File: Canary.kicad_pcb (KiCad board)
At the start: 4 copper layers, 56 x 38 mm, 92 parts, among them J1 CONN_ARM_CM_JTAG_SWD_10, J2 20021311-00010T4LF, J3 USB4125-GF-A, J4 S2B-PH-SM4-TB, Q1 PMN30UNX, Q2 PMN42XPEAH, Q3 PMN30UNX, SW1 TL3301SPF160QJ, U1 BMD-300-A-R, U10 LP5907MFX-3.2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

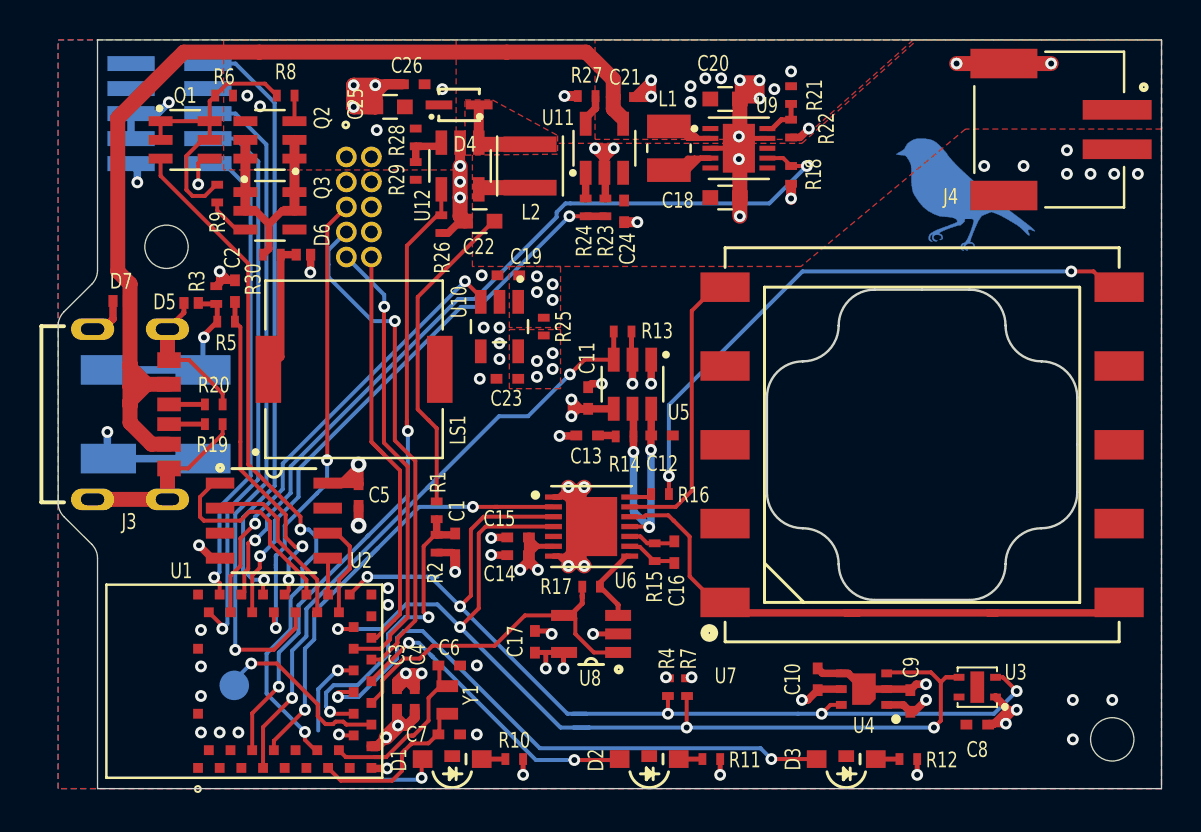
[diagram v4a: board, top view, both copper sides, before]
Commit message: Clean up silks, add fiducials
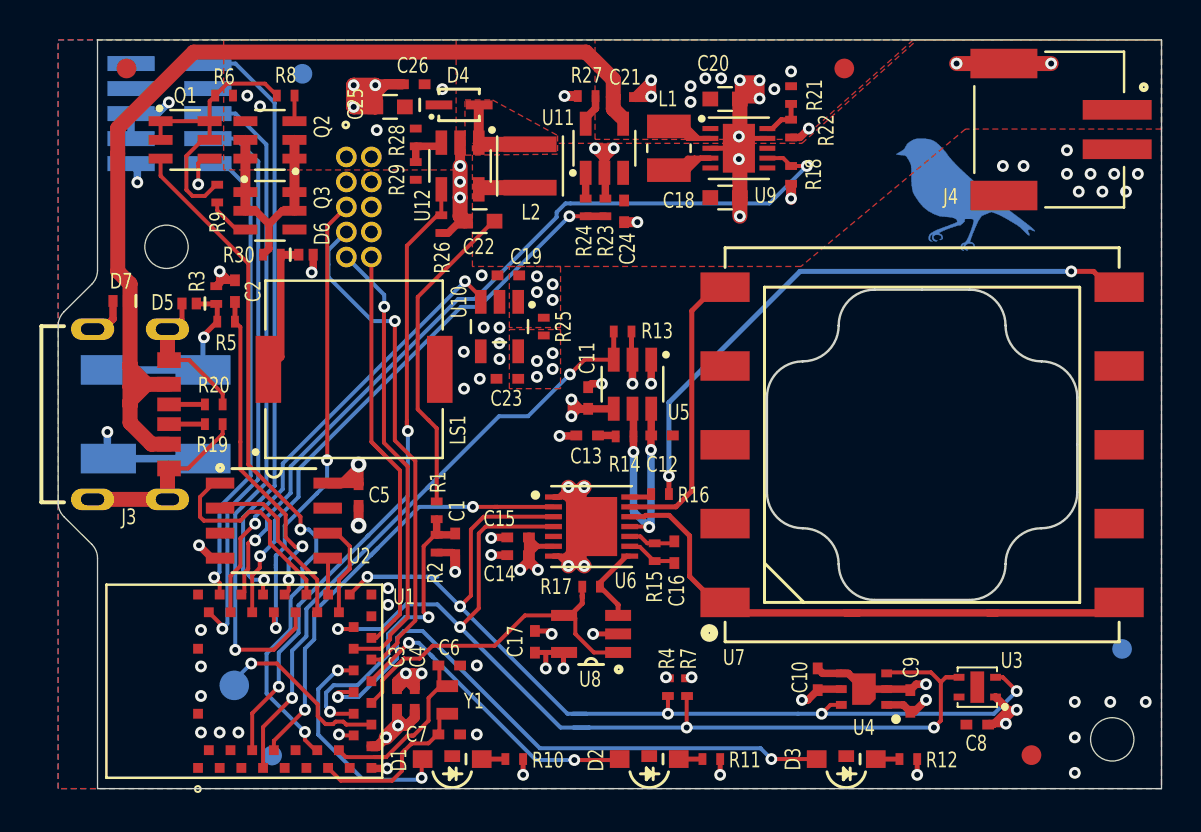
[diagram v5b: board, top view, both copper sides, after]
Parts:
- added FID1: Fiducial, Fiducials:Fiducial_1mm_Dia_2mm_Outer, F.Cu at (80.9, 49.5)
- added FID2: Fiducial, Fiducials:Fiducial_1mm_Dia_2mm_Outer, F.Cu at (90.4, 84.3)
- added FID3: Fiducial, Fiducials:Fiducial_1mm_Dia_2mm_Outer, F.Cu at (44.5, 49.5)
- added FID4: Fiducial, Fiducials:Fiducial_1mm_Dia_2mm_Outer, B.Cu at (95.0, 78.9)
- added FID5: Fiducial, Fiducials:Fiducial_1mm_Dia_2mm_Outer, B.Cu at (51.9, 84.3)
- added FID6: Fiducial, Fiducials:Fiducial_1mm_Dia_2mm_Outer, B.Cu at (53.4, 49.7)
- moved D6 0.13 mm to (53.6, 58.9)
- moved D5 0.10 mm to (47.6, 61.4)
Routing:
- net VBUS: track 57.8 -> 53.3 mm
- net LED_GREEN: track 8.06 -> 11.9 mm
- net /Potentiostat/SPEC_WE: track 29.0 -> 31.4 mm
- net /Potentiostat/SPEC_RE: track 14.4 -> 16.6 mm
- net /Potentiostat/SPEC_CE: track 30.1 -> 31.8 mm
- net /PDRIVE_O: track 8.26 -> 9.18 mm
- net GND: track 122.9 -> 123.0 mm, vias 75 -> 82

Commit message: Prepare for fab export
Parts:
- moved S1 0.43 mm to (50.3, 48.5)

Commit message: Generate gerbers
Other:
- rule pad_to_mask_clearance: 0.05 -> 0

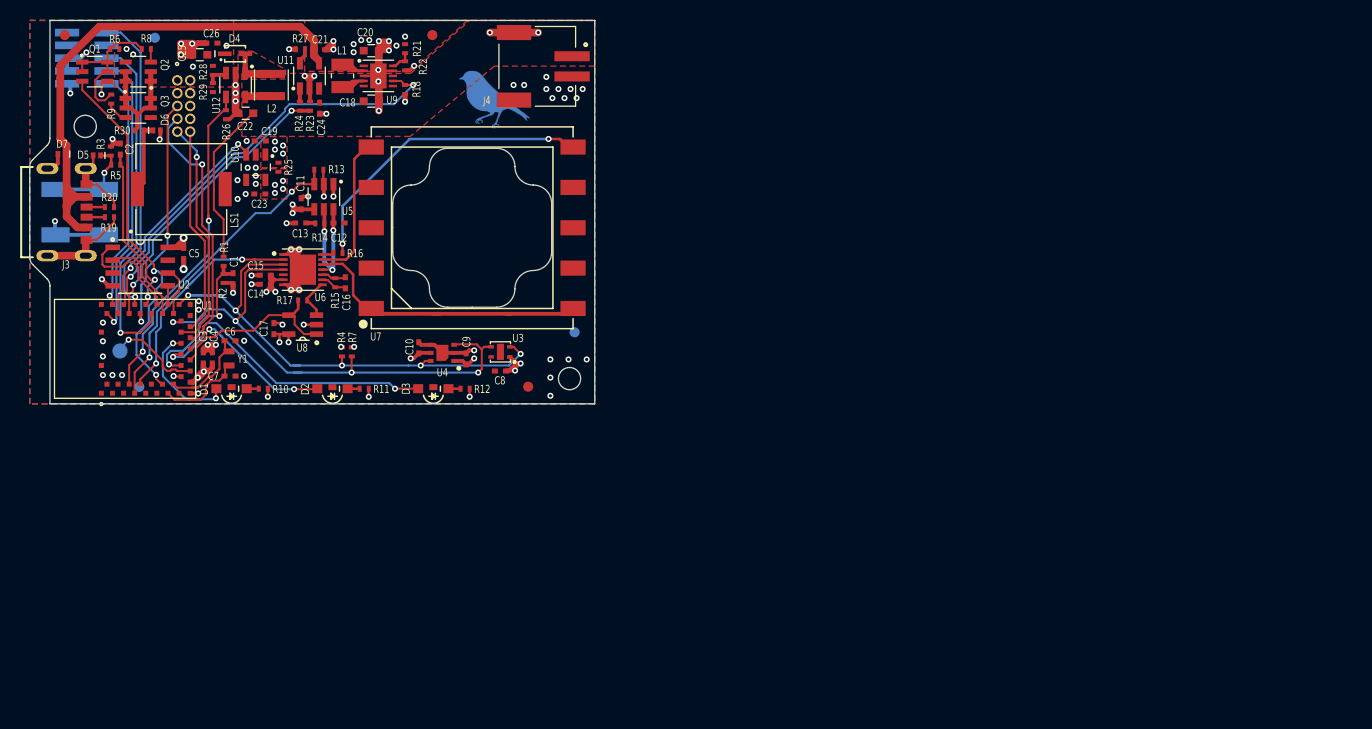
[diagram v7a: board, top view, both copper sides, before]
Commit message: Regenerate Gerbers using PCBWay process
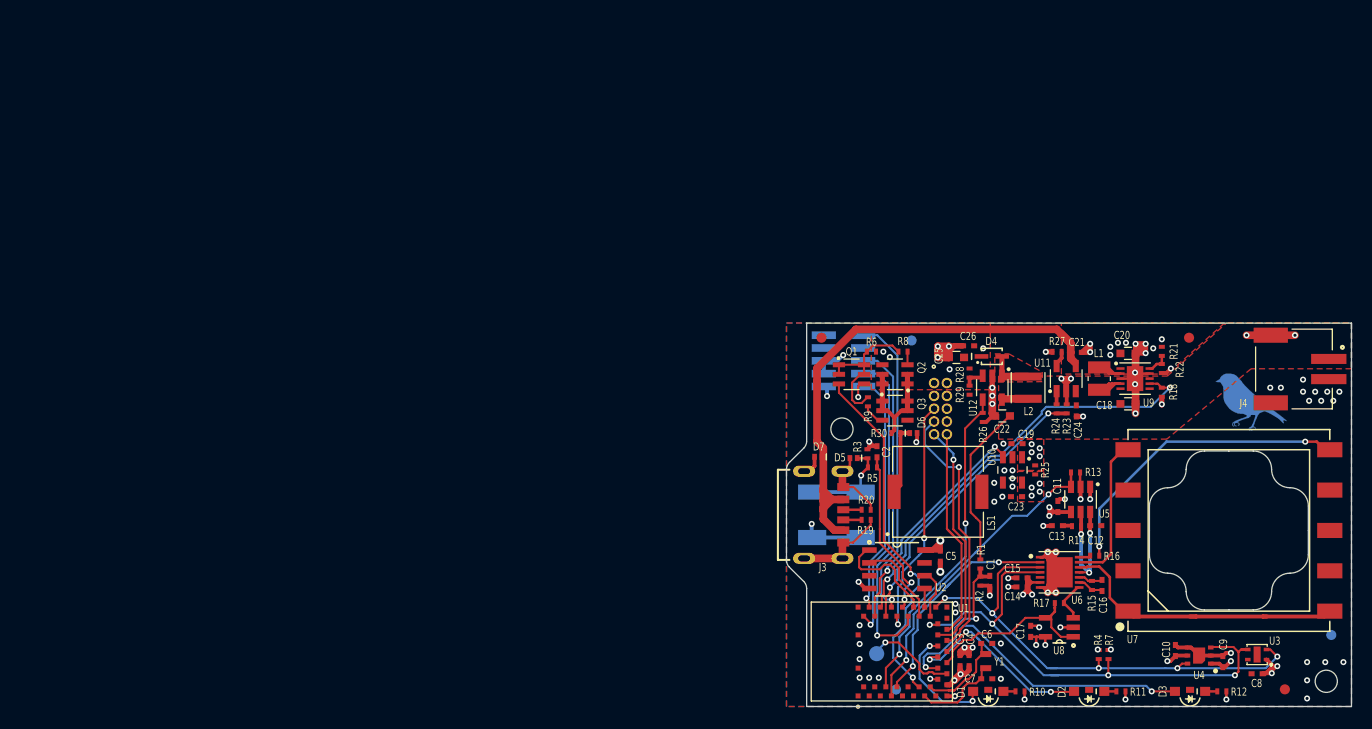
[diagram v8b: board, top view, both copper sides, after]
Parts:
- moved D6 80.8 mm to (128.6, 88.9)
- moved C1 80.8 mm to (136.2, 103.6)
- moved C10 80.8 mm to (154.6, 110.5)
- moved C11 80.8 mm to (142.9, 96.2)
- moved C12 80.8 mm to (146.7, 98.1)
- moved C13 80.8 mm to (142.8, 98.1)
- moved C14 80.8 mm to (139.3, 104.2)
- moved C15 80.8 mm to (139.3, 103.2)
- moved C16 80.8 mm to (147.3, 104.0)
- moved C18 80.8 mm to (149.8, 86.0)
- moved C19 80.8 mm to (138.8, 90.0)
- moved C2 80.8 mm to (125.0, 90.8)
- moved C20 80.8 mm to (149.8, 81.0)
- moved C21 80.8 mm to (144.7, 80.9)
- moved C22 80.8 mm to (137.4, 87.2)
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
